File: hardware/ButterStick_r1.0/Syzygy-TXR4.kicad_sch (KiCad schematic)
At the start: 19 parts, among them J5 SYZYGY-TXR-4, U15 TLV62569DRL

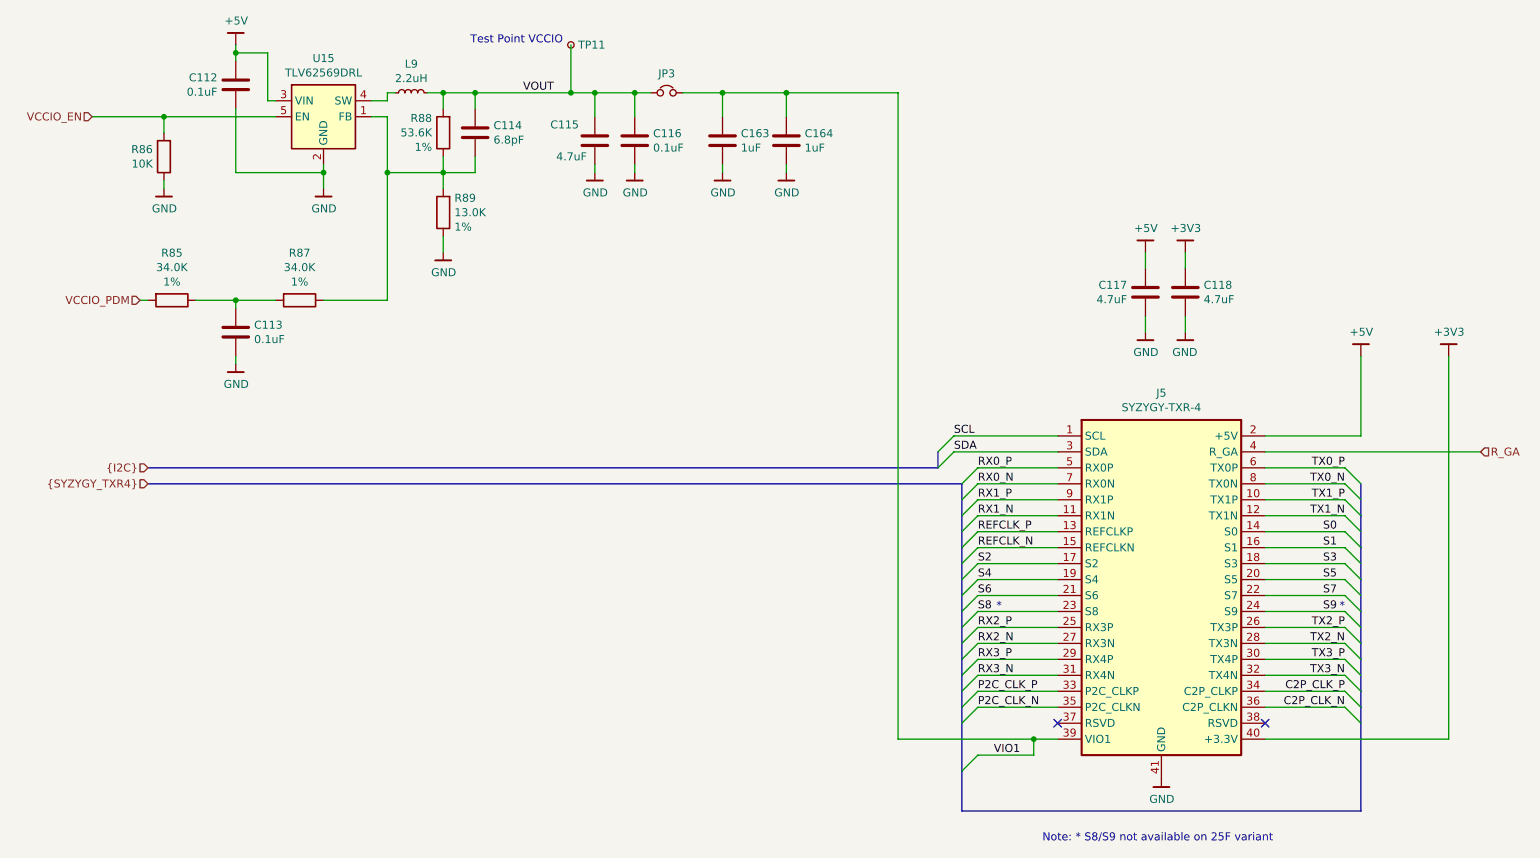
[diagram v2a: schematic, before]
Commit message: hw.r1d0: Fix RGMII straps
This commit correctly sets the stop resistos on the RGMII lines to 1K5
instead of DNP.
Also regenerate and add a schematic in PDF format.

Fixes #6
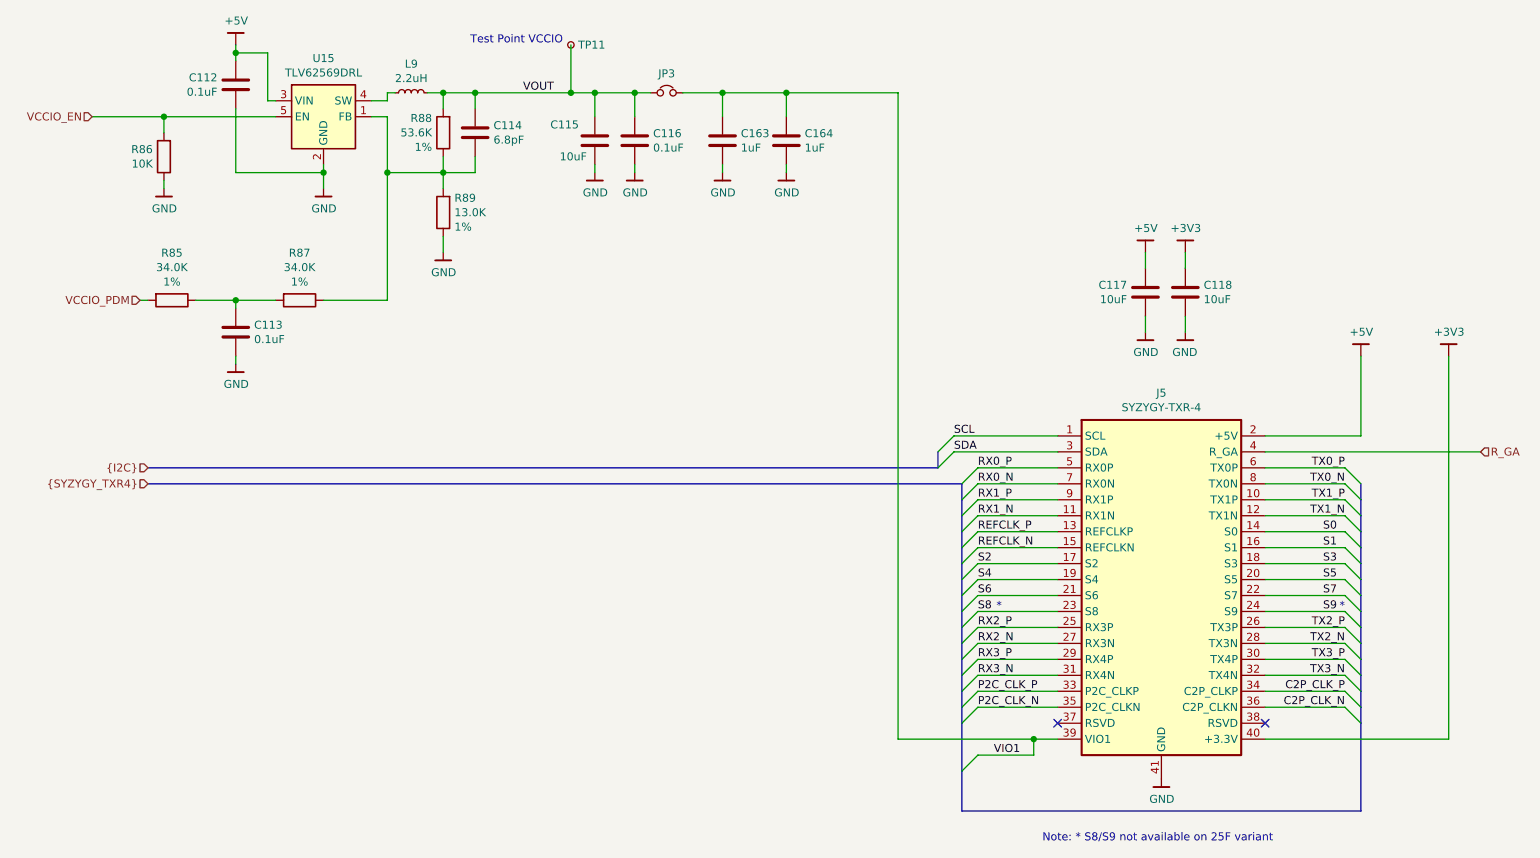
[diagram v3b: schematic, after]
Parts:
- C115, C117, C118: value 4.7uF -> 10uF; PN CC0603ZRY5V6BB475 -> CC0603KRX5R5BB106
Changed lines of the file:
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@@
-(kicad_sch (version 20200618) (host eeschema "5.99.0-unknown-73168a9~101~ubuntu18.04.1")
+(kicad_sch (version 20201015) (generator eeschema)
   (page 1 18)
   (paper "A4")
   (title_block
     (title "ButterStick")
-    (date "2020-07-17")
+    (date "2020-11-01")
     (rev "r1.0")
     (company "GsD")
     (comment 1 "Functional prototyping board for the Lattice ECP5.")
-  )
-  (junction (at 38.1 43.18) (diameter 0) (color 0 0 0 0))
-  (junction (at 49.53 33.02) (diameter 0) (color 0 0 0 0))
-  (junction (at 49.53 72.39) (diameter 0) (color 0 0 0 0))
-  (junction (at 63.5 52.07) (diameter 0) (color 0 0 0 0))
-  (junction (at 73.66 52.07) (diameter 0) (color 0 0 0 0))
-  (junction (at 82.55 39.37) (diameter 0) (color 0 0 0 0))
-  (junction (at 82.55 52.07) (diameter 0) (color 0 0 0 0))
-  (junction (at 87.63 39.37) (diameter 0) (color 0 0 0 0))
-  (junction (at 102.87 39.37) (diameter 0) (color 0 0 0 0))
-  (junction (at 106.68 39.37) (diameter 0) (color 0 0 0 0))
-  (junction (at 113.03 39.37) (diameter 0) (color 0 0 0 0))
-  (junction (at 127 39.37) (diameter 0) (color 0 0 0 0))
-  (junction (at 137.16 39.37) (diameter 0) (color 0 0 0 0))
-  (junction (at 176.53 142.24) (diameter 0) (color 0 0 0 0))
+    (comment 2 "SYZYGY compatible")
+  )
+  (junction (at 38.1 43.18) (diameter 1.016) (color 0 0 0 0))
+  (junction (at 49.53 33.02) (diameter 1.016) (color 0 0 0 0))
+  (junction (at 49.53 72.39) (diameter 1.016) (color 0 0 0 0))
+  (junction (at 63.5 52.07) (diameter 1.016) (color 0 0 0 0))
+  (junction (at 73.66 52.07) (diameter 1.016) (color 0 0 0 0))
+  (junction (at 82.55 39.37) (diameter 1.016) (color 0 0 0 0))
+  (junction (at 82.55 52.07) (diameter 1.016) (color 0 0 0 0))
+  (junction (at 87.63 39.37) (diameter 1.016) (color 0 0 0 0))
+  (junction (at 102.87 39.37) (diameter 1.016) (color 0 0 0 0))
+  (junction (at 106.68 39.37) (diameter 1.016) (color 0 0 0 0))
+  (junction (at 113.03 39.37) (diameter 1.016) (color 0 0 0 0))
+  (junction (at 127 39.37) (diameter 1.016) (color 0 0 0 0))
+  (junction (at 137.16 39.37) (diameter 1.016) (color 0 0 0 0))
+  (junction (at 176.53 142.24) (diameter 1.016) (color 0 0 0 0))
+  (no_connect (at 213.36 139.7))
   (no_connect (at 180.34 139.7))
-  (no_connect (at 213.36 139.7))
   (bus_entry (at 161.29 96.52) (size 2.54 -2.54)
     (stroke (width 0.1524) (type solid) (color 0 0 0 0))
@@
     (stroke (width 0) (type solid) (color 0 0 0 0))
   )
-  (bus (pts (xy 165.1 101.6) (xy 165.1 106.68))
-    (stroke (width 0) (type solid) (color 0 0 0 0))
-  )
-  (bus (pts (xy 165.1 106.68) (xy 165.1 111.76))
-    (stroke (width 0) (type solid) (color 0 0 0 0))
-  )
-  (bus (pts (xy 165.1 111.76) (xy 165.1 116.84))
-    (stroke (width 0) (type solid) (color 0 0 0 0))
-  )
-  (bus (pts (xy 165.1 116.84) (xy 165.1 121.92))
+  (bus (pts (xy 165.1 101.6) (xy 165.1 104.14))
+    (stroke (width 0) (type solid) (color 0 0 0 0))
+  )
+  (bus (pts (xy 165.1 104.14) (xy 165.1 106.68))
+    (stroke (width 0) (type solid) (color 0 0 0 0))
+  )
+  (bus (pts (xy 165.1 106.68) (xy 165.1 109.22))
+    (stroke (width 0) (type solid) (color 0 0 0 0))
+  )
+  (bus (pts (xy 165.1 109.22) (xy 165.1 111.76))
+    (stroke (width 0) (type solid) (color 0 0 0 0))
+  )
+  (bus (pts (xy 165.1 111.76) (xy 165.1 114.3))
+    (stroke (width 0) (type solid) (color 0 0 0 0))
+  )
+  (bus (pts (xy 165.1 114.3) (xy 165.1 116.84))
+    (stroke (width 0) (type solid) (color 0 0 0 0))
+  )
+  (bus (pts (xy 165.1 116.84) (xy 165.1 119.38))
+    (stroke (width 0) (type solid) (color 0 0 0 0))
+  )
+  (bus (pts (xy 165.1 119.38) (xy 165.1 121.92))
     (stroke (width 0) (type solid) (color 0 0 0 0))
   )
@@
     (stroke (width 0) (type solid) (color 0 0 0 0))
   )
-  (bus (pts (xy 165.1 124.46) (xy 165.1 129.54))
+  (bus (pts (xy 165.1 124.46) (xy 165.1 127))
+    (stroke (width 0) (type solid) (color 0 0 0 0))
+  )
+  (bus (pts (xy 165.1 127) (xy 165.1 129.54))
     (stroke (width 0) (type solid) (color 0 0 0 0))
   )
@@
     (stroke (width 0) (type solid) (color 0 0 0 0))
   )
-  (bus (pts (xy 165.1 132.08) (xy 165.1 137.16))
-    (stroke (width 0) (type solid) (color 0 0 0 0))
-  )
-  (bus (pts (xy 165.1 137.16) (xy 165.1 147.32))
+  (bus (pts (xy 165.1 132.08) (xy 165.1 134.62))
+    (stroke (width 0) (type solid) (color 0 0 0 0))
+  )
+  (bus (pts (xy 165.1 134.62) (xy 165.1 137.16))
+    (stroke (width 0) (type solid) (color 0 0 0 0))
+  )
+  (bus (pts (xy 165.1 137.16) (xy 165.1 139.7))
+    (stroke (width 0) (type solid) (color 0 0 0 0))
+  )
+  (bus (pts (xy 165.1 139.7) (xy 165.1 147.32))
     (stroke (width 0) (type solid) (color 0 0 0 0))
   )
@@
     (stroke (width 0) (type solid) (color 0 0 0 0))
   )
-  (bus (pts (xy 228.6 101.6) (xy 228.6 106.68))
-    (stroke (width 0) (type solid) (color 0 0 0 0))
-  )
-  (bus (pts (xy 228.6 106.68) (xy 228.6 111.76))
-    (stroke (width 0) (type solid) (color 0 0 0 0))
-  )
-  (bus (pts (xy 228.6 111.76) (xy 228.6 116.84))
-    (stroke (width 0) (type solid) (color 0 0 0 0))
-  )
-  (bus (pts (xy 228.6 116.84) (xy 228.6 121.92))
-    (stroke (width 0) (type solid) (color 0 0 0 0))
-  )
-  (bus (pts (xy 228.6 121.92) (xy 228.6 127))
+  (bus (pts (xy 228.6 101.6) (xy 228.6 104.14))
+    (stroke (width 0) (type solid) (color 0 0 0 0))
+  )
+  (bus (pts (xy 228.6 104.14) (xy 228.6 106.68))
+    (stroke (width 0) (type solid) (color 0 0 0 0))
+  )
+  (bus (pts (xy 228.6 106.68) (xy 228.6 109.22))
+    (stroke (width 0) (type solid) (color 0 0 0 0))
+  )
+  (bus (pts (xy 228.6 109.22) (xy 228.6 111.76))
+    (stroke (width 0) (type solid) (color 0 0 0 0))
+  )
+  (bus (pts (xy 228.6 111.76) (xy 228.6 114.3))
+    (stroke (width 0) (type solid) (color 0 0 0 0))
+  )
+  (bus (pts (xy 228.6 114.3) (xy 228.6 116.84))
+    (stroke (width 0) (type solid) (color 0 0 0 0))
+  )
+  (bus (pts (xy 228.6 116.84) (xy 228.6 119.38))
+    (stroke (width 0) (type solid) (color 0 0 0 0))
+  )
+  (bus (pts (xy 228.6 119.38) (xy 228.6 121.92))
+    (stroke (width 0) (type solid) (color 0 0 0 0))
+  )
+  (bus (pts (xy 228.6 121.92) (xy 228.6 124.46))
+    (stroke (width 0) (type solid) (color 0 0 0 0))
+  )
+  (bus (pts (xy 228.6 124.46) (xy 228.6 127))
     (stroke (width 0) (type solid) (color 0 0 0 0))
   )
@@
     (stroke (width 0) (type solid) (color 0 0 0 0))
   )
-  (bus (pts (xy 228.6 129.54) (xy 228.6 134.62))
+  (bus (pts (xy 228.6 129.54) (xy 228.6 132.08))
+    (stroke (width 0) (type solid) (color 0 0 0 0))
+  )
+  (bus (pts (xy 228.6 132.08) (xy 228.6 134.62))
     (stroke (width 0) (type solid) (color 0 0 0 0))
   )
@@
     (stroke (width 0) (type solid) (color 0 0 0 0))
   )
-  (bus (pts (xy 228.6 137.16) (xy 228.6 153.67))
+  (bus (pts (xy 228.6 137.16) (xy 228.6 139.7))
+    (stroke (width 0) (type solid) (color 0 0 0 0))
+  )
+  (bus (pts (xy 228.6 139.7) (xy 228.6 153.67))
     (stroke (width 0) (type solid) (color 0 0 0 0))
   )
@@
       (effects (font (size 1.27 1.27)) (justify right))
     )
-    (property "Value" "4.7uF" (id 1) (at 105.41 49.53 0)
+    (property "Value" "10uF" (id 1) (at 105.41 49.53 0)
       (effects (font (size 1.27 1.27)) (justify right))
     )
@@
       (effects (font (size 1.27 1.27)) hide)
     )
-    (property "PN" "CC0603ZRY5V6BB475" (id 5) (at -13.97 179.07 0)
+    (property "PN" "CC0603KRX5R5BB106" (id 5) (at -13.97 179.07 0)
       (effects (font (size 1.27 1.27)) hide)
     )
@@
       (effects (font (size 1.27 1.27)) (justify right))
     )
-    (property "Value" "4.7uF" (id 1) (at 191.389 72.263 0)
+    (property "Value" "10uF" (id 1) (at 191.389 72.263 0)
       (effects (font (size 1.27 1.27)) (justify right))
     )
@@
       (effects (font (size 1.27 1.27)) hide)
     )
-    (property "PN" "CC0603ZRY5V6BB475" (id 5) (at 73.66 203.2 0)
+    (property "PN" "CC0603KRX5R5BB106" (id 5) (at 73.66 203.2 0)
       (effects (font (size 1.27 1.27)) hide)
     )
@@
       (effects (font (size 1.27 1.27)) (justify right))
     )
-    (property "Value" "4.7uF" (id 1) (at 203.581 72.263 0)
+    (property "Value" "10uF" (id 1) (at 203.581 72.263 0)
       (effects (font (size 1.27 1.27)) (justify right))
     )
@@
       (effects (font (size 1.27 1.27)) hide)
     )
-    (property "PN" "CC0603ZRY5V6BB475" (id 5) (at 321.31 203.2 0)
-      (effects (font (size 1.27 1.27)) hide)
-    )
+    (property "PN" "CC0603KRX5R5BB106" (id 5) (at 321.31 203.2 0)
+      (effects (font (size 1.27 1.27)) hide)
+    )

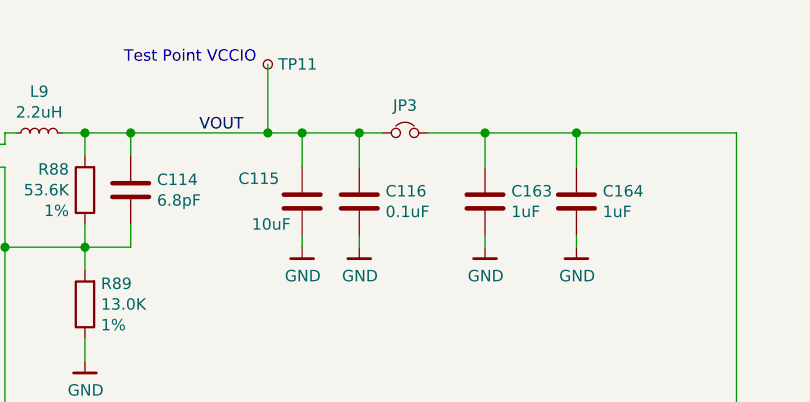
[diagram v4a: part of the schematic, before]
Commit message: hardware.r1d0: Tidy up BOM entries
Export HTML Interactive BOM
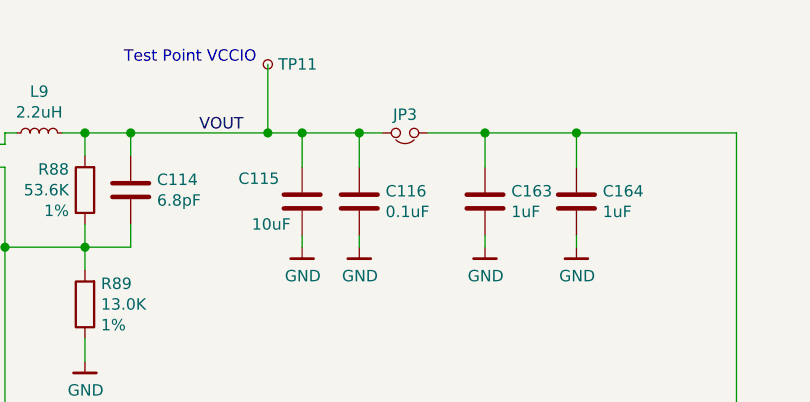
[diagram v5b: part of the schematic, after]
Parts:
- JP3: now left out of the parts list
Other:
- moved on the sheet: JP3
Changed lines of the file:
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@@
   (junction (at 137.16 39.37) (diameter 1.016) (color 0 0 0 0))
   (junction (at 176.53 142.24) (diameter 1.016) (color 0 0 0 0))
+  (no_connect (at 213.36 139.7))
   (no_connect (at 180.34 139.7))
-  (no_connect (at 213.36 139.7))
   (bus_entry (at 161.29 96.52) (size 2.54 -2.54)
     (stroke (width 0.1524) (type solid) (color 0 0 0 0))
@@
     )
   )
-  (symbol (lib_id "Device:Jumper_NC_Small") (at 118.11 39.37 0) (unit 1)
-    (in_bom yes) (on_board yes)
-    (property "Reference" "JP3" (id 0) (at 118.11 36.322 0))
-    (property "Value" "Jumper_NC" (id 1) (at 118.11 36.322 0)
-      (effects (font (size 1.27 1.27)) hide)
-    )
+  (symbol (lib_id "Device:Jumper_NC_Small") (at 118.11 39.37 0) (mirror x) (unit 1)
+    (in_bom no) (on_board yes)
+    (property "Reference" "JP3" (id 0) (at 118.11 37.338 0))
+    (property "Value" "Jumper_NC" (id 1) (at 118.11 42.418 0)
+      (effects (font (size 1.27 1.27)) hide)
+    )

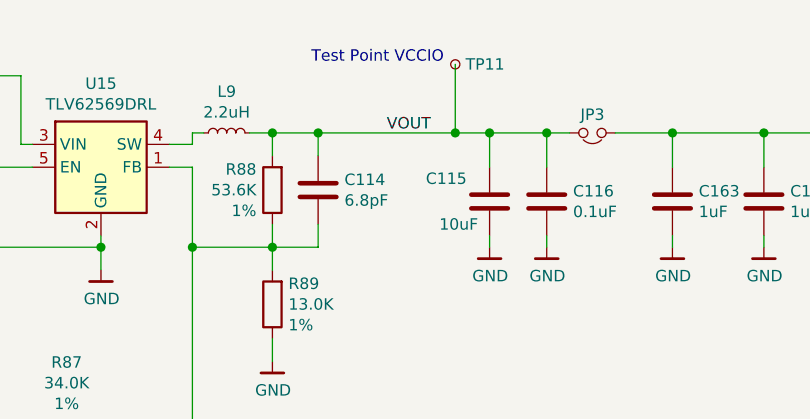
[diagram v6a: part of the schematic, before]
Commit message: Fix RGB G/B signals
- Corrects a mistake where blue and green signals were swapped
- Regenerate schematic

Closes #12
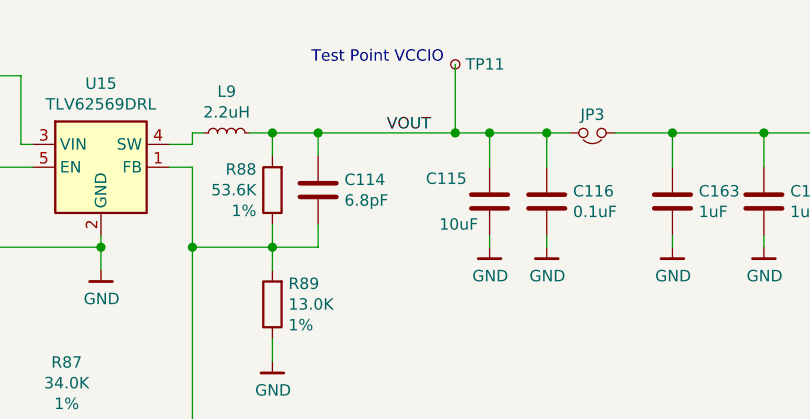
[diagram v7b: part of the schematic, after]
